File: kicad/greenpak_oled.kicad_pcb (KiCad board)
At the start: 2 copper layers, 35.6 x 35.6 mm, 21 parts, among them J1 Conn_01x05_Pin, J3 POGO_SOCKET, U1 SLG46826G, U2 OLED-128O064D

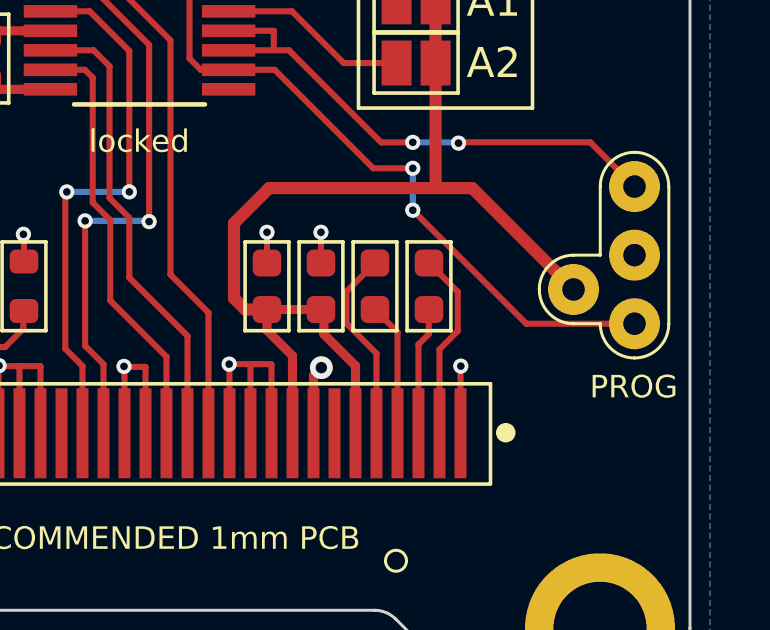
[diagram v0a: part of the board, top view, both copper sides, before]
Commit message: Tweaked the schematic to match also SH1106.
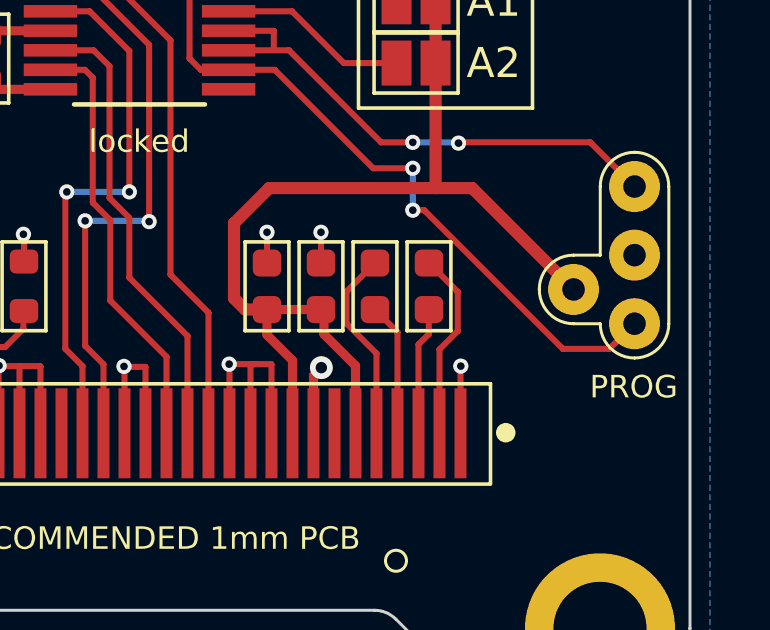
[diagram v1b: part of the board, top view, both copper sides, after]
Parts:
- C3: value 2u2 -> 4u7
- C6: value 100n -> 2u2
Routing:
- net Net-(J3-SDA): track 24.0 -> 24.7 mm
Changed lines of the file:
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@@
         (effects (font (size 1 1) (thickness 0.15)))
     )
-    (fp_text value "100n" (at 0 1.43 -90) (layer "F.Fab") hide
+    (fp_text value "2u2" (at 0 1.43 -90) (layer "F.Fab") hide
         (effects (font (size 1 1) (thickness 0.15)))
     )
@@
         (effects (font (size 1 1) (thickness 0.15)))
     )
-    (fp_text value "2u2" (at 0 1.43 -90) (layer "F.Fab") hide
+    (fp_text value "4u7" (at 0 1.43 -90) (layer "F.Fab") hide
         (effects (font (size 1 1) (thickness 0.15)))
     )
@@
     (effects (font (size 0.75 0.75) (thickness 0.1)) (justify mirror))
   )
-  (gr_text locked "1.3{dblquote} OLED\nSSD1306\n" (at -0.508 -4.191) (layer "B.SilkS")
+  (gr_text locked "1.3{dblquote} OLED" (at -0.508 -4.191) (layer "B.SilkS")
     (effects (font (size 1.5 1.5) (thickness 0.2)) (justify mirror))
   )
@@
     (effects (font (size 0.75 0.75) (thickness 0.1)))
   )
-  (gr_text locked "GREENPAK\nADDRESSABLE\nSPI OLED\nSSD1306\n3.3V\nADDR 0-7\nJMPR=1\nV 0.2" (at -16.4846 -10.1346) (layer "F.SilkS")
+  (gr_text locked "GREENPAK\nADDRESSABLE\nSPI OLED\nADDR 0-7\nJMPR=1\n3.3V\nV 0.2\n" (at -16.4846 -10.1346) (layer "F.SilkS")
     (effects (font (size 1 1) (thickness 0.15)) (justify left top))
   )
@@
     (effects (font (size 0.75 0.75) (thickness 0.1)))
   )
+  (segment (start 3.7 5.0208) (end 3.7 4.175) (width 0.3048) (layer "F.Cu") (net 1))
   (segment (start 9.3472 0.127) (end 9.319099 0.098899) (width 0.4064) (layer "F.Cu") (net 1))
-  (segment (start 4.55 5.7184) (end 3.7 4.8684) (width 0.3048) (layer "F.Cu") (net 1))
   (segment (start 9.319099 -9.934101) (end 7.2136 -12.0396) (width 0.4064) (layer "F.Cu") (net 1))
   (segment (start -3.451251 -5.115702) (end -5.7419 -5.115702) (width 0.3048) (layer "F.Cu") (net 1))
   (segment (start 2.975 4.175) (end 2.6 3.8) (width 0.4064) (layer "F.Cu") (net 1))
   (segment (start 6.65 7.8) (end 6.65 6.05) (width 0.3048) (layer "F.Cu") (net 1))
+  (segment (start 4.55 5.8708) (end 3.7 5.0208) (width 0.3048) (layer "F.Cu") (net 1))
   (segment (start 5.5 4.175) (end 3.7 4.175) (width 0.3048) (layer "F.Cu") (net 1))
   (segment (start 3.7 4.175) (end 2.975 4.175) (width 0.4064) (layer "F.Cu") (net 1))
@@
   (segment (start 3.773 0.127) (end 10.541 0.127) (width 0.4064) (layer "F.Cu") (net 1))
   (segment (start 4.5466 -12.3444) (end -4.3942 -12.3444) (width 0.4064) (layer "F.Cu") (net 1))
-  (segment (start 4.55 7.8) (end 4.55 5.7184) (width 0.3048) (layer "F.Cu") (net 1))
   (segment (start 4.562299 -12.328701) (end 4.5466 -12.3444) (width 0.4064) (layer "F.Cu") (net 1))
   (segment (start 10.541 0.127) (end 13.9192 3.5052) (width 0.4064) (layer "F.Cu") (net 1))
+  (segment (start 4.55 7.8) (end 4.55 5.8708) (width 0.3048) (layer "F.Cu") (net 1))
   (segment (start 2.352649 -9.015699) (end 4.406497 -9.015699) (width 0.3048) (layer "F.Cu") (net 1))
   (segment (start 7.2136 -12.0396) (end 6.9088 -12.3444) (width 0.4064) (layer "F.Cu") (net 1))
@@
   (segment (start 2.6 1.3) (end 3.773 0.127) (width 0.4064) (layer "F.Cu") (net 1))
   (segment (start -5.6388 -11.0998) (end -5.6388 -5.0546) (width 0.4064) (layer "F.Cu") (net 1))
-  (segment (start 3.7 4.8684) (end 3.7 4.175) (width 0.3048) (layer "F.Cu") (net 1))
   (segment (start -4.3942 -12.3444) (end -5.6388 -11.0998) (width 0.4064) (layer "F.Cu") (net 1))
   (segment (start 6.65 6.05) (end 5.6 5) (width 0.3048) (layer "F.Cu") (net 1))
@@
   (segment (start -2.6 -13.1064) (end -2.6 -11.116) (width 0.2032) (layer "B.Cu") (net 11))
   (segment (start -2.6 -11.116) (end -2.6162 -11.0998) (width 0.2032) (layer "B.Cu") (net 11))
-  (segment (start 15.9512 4.6482) (end 12.344402 4.6482) (width 0.2032) (layer "F.Cu") (net 12))
+  (segment (start 15.9512 4.6482) (end 15.113 5.4864) (width 0.2032) (layer "F.Cu") (net 12))
+  (segment (start 8.9408 0.8636) (end 8.559802 0.8636) (width 0.2032) (layer "F.Cu") (net 12))
   (segment (start 1.314899 -7.715699) (end 1.1176 -7.5184) (width 0.2032) (layer "F.Cu") (net 12))
   (segment (start 1.1176 -7.5184) (end 1.1176 -4.193498) (width 0.2032) (layer "F.Cu") (net 12))
+  (segment (start 13.5636 5.4864) (end 8.9408 0.8636) (width 0.2032) (layer "F.Cu") (net 12))
   (segment (start 3.956701 -3.815699) (end 7.239 -0.5334) (width 0.2032) (layer "F.Cu") (net 12))
   (segment (start 1.1176 -4.193498) (end 1.495399 -3.815699) (width 0.2032) (layer "F.Cu") (net 12))
-  (segment (start 12.344402 4.6482) (end 8.559802 0.8636) (width 0.2032) (layer "F.Cu") (net 12))
   (segment (start 1.495399 -3.815699) (end 3.956701 -3.815699) (width 0.2032) (layer "F.Cu") (net 12))
   (segment (start 2.352649 -7.715699) (end 1.314899 -7.715699) (width 0.2032) (layer "F.Cu") (net 12))
+  (segment (start 15.113 5.4864) (end 13.5636 5.4864) (width 0.2032) (layer "F.Cu") (net 12))
   (segment (start 7.239 -0.5334) (end 8.5598 -0.5334) (width 0.2032) (layer "F.Cu") (net 12))
   (via (at 8.559802 0.8636) (size 0.508) (drill 0.254) (layers "F.Cu" "B.Cu") (net 12))
